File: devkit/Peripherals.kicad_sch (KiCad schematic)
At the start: 50 parts, among them IC501 APDS-9306-065, IC502 BMI270, IC503 LIS2MDLTR, IC504 BMP581, IC505 DRV2603RUNT, IC506 PCA9306JK, IC507 RV-8263-C8, J501 Jumper, J502 Jumper, J503 Jumper, J504 Jumper, J505 Jumper, J506 Jumper, J507 Jumper, M501 Vibrator DC Motor, X501 Current, X502 I2S, X503 Current, X504 I2C, X505 Current, X506 Current, X507 Current, X508 Current, X509 Motor, X510 Current

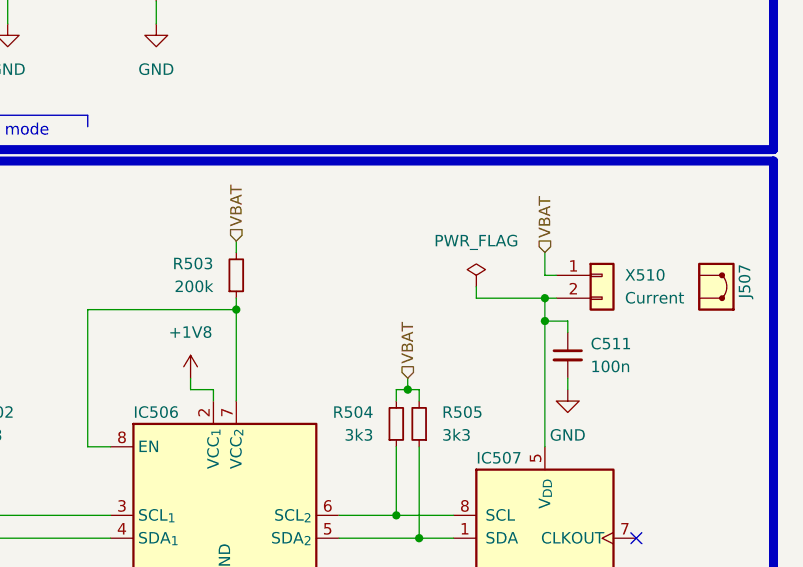
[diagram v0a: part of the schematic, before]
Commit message: Feature: Issue #186
Allow powering RTC from any voltage source

Closes #186

Signed-off-by: Daniel Kampert <DanielKampert@kampis-elektroecke.de>
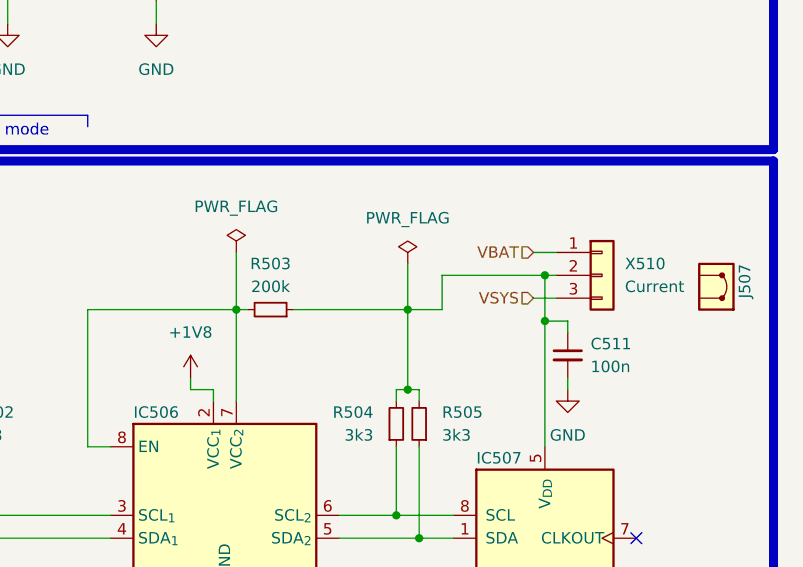
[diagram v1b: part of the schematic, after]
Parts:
- X510: footprint Connector_PinHeader_2.54mm:PinHeader_1x02_P2.54mm_Vertical -> Connector_PinHeader_2.54mm:PinHeader_1x03_P2.54mm_Vertical; symbol Connector_Generic:Conn_01x02 -> Connector_Generic:Conn_01x03; manf# 77311-818-02LF -> 77311-818-03LF; mouser# 649-77311-818-02LF -> 649-77311-818-03LF
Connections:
- net VBAT: no longer R503.2, R504.2, R505.2
- net VSYS: now also X510.3 (Pin_3)
- net at C511.1, IC507.5 (V_{DD}), X510.2 (Pin_2): now also R503.1, R504.2, R505.2
- net at IC506.7 (VCC_{2}), IC506.8 (EN): now also R503.2; no longer R503.1
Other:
- moved on the sheet: R503

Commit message: Revert "Feature: Issue #186"
This reverts commit 73512b60dac517a3d61ff56758c38d705b52f64d.
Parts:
- X510: footprint Connector_PinHeader_2.54mm:PinHeader_1x03_P2.54mm_Vertical -> Connector_PinHeader_2.54mm:PinHeader_1x02_P2.54mm_Vertical; symbol Connector_Generic:Conn_01x03 -> Connector_Generic:Conn_01x02; manf# 77311-818-03LF -> 77311-818-02LF; mouser# 649-77311-818-03LF -> 649-77311-818-02LF
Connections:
- net VBAT: now also R503.2, R504.2, R505.2
- net VSYS: no longer X510.3 (Pin_3)
- net at C511.1, IC507.5 (V_{DD}), X510.2 (Pin_2): no longer R503.1, R504.2, R505.2
- net at IC506.7 (VCC_{2}), IC506.8 (EN): now also R503.1; no longer R503.2
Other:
- moved on the sheet: R503

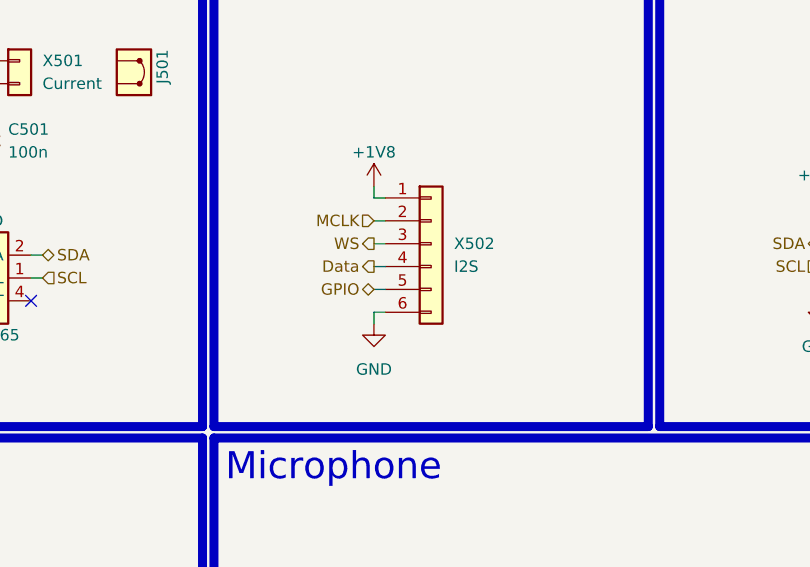
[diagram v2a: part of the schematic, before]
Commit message: Revert "Feature: Issue #180"
This reverts commit 364f4bbc8b17cbfb7f0155205af3315526997ba0.
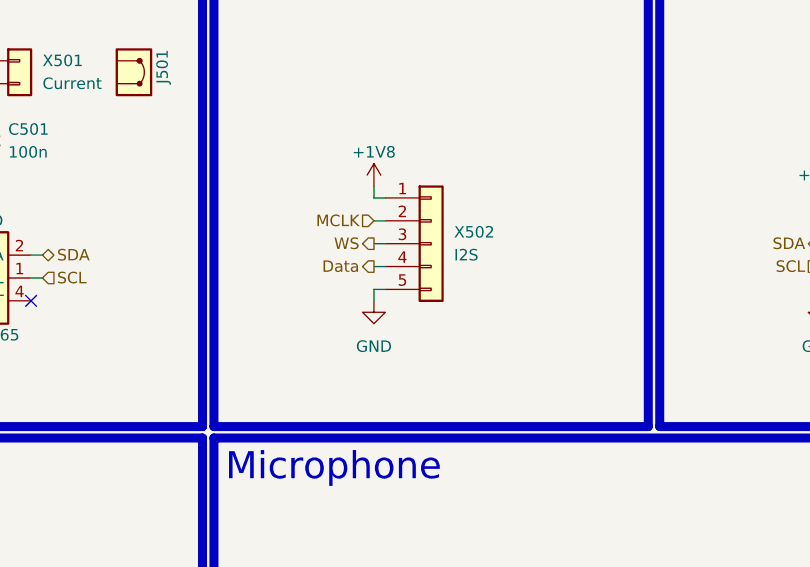
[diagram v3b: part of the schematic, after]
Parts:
- X502: footprint Connector_PinHeader_2.54mm:PinHeader_1x06_P2.54mm_Vertical -> Connector_PinHeader_2.54mm:PinHeader_1x05_P2.54mm_Vertical; symbol Connector_Generic:Conn_01x06 -> Connector_Generic:Conn_01x05; manf# 77311-818-06LF -> 77311-818-05LF; mouser# 649-77311-818-06LF -> 649-77311-818-05LF
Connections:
- net GPIO is gone; now on net GND: X502.5 (Pin_5)
- net GND: no longer X502.6 (Pin_6)
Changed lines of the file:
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@@
 	(wire
 		(pts
-			(xy 80.01 58.42) (xy 78.74 58.42)
+			(xy 80.01 55.88) (xy 78.74 55.88)
 		)
 		(stroke
@@
 	(wire
 		(pts
-			(xy 78.74 58.42) (xy 78.74 59.69)
+			(xy 78.74 55.88) (xy 78.74 57.15)
 		)
 		(stroke
@@
 	(wire
 		(pts
-			(xy 78.74 55.88) (xy 80.01 55.88)
-		)
-		(stroke
-			(width 0)
-			(type default)
-		)
-	)
-	(wire
-		(pts
 			(xy 20.32 111.76) (xy 19.05 111.76)
 		)
@@
 		)
 	)
-	(hierarchical_label "GPIO"
-		(shape bidirectional)
-		(at 78.74 55.88 180)
-		(effects
-			(font
-				(size 1.27 1.27)
-			)
-			(justify right)
-		)
-	)
 	(hierarchical_label "SDA"
 		(shape bidirectional)
@@
 	)
 	(symbol
-		(lib_id "Connector_Generic:Conn_01x06")
+		(lib_id "Connector_Generic:Conn_01x05")
 		(at 85.09 50.8 0)
 		(unit 1)
@@
 		(fields_autoplaced yes)
 		(property "Reference" "X502"
-			(at 87.63 50.7999 0)
+			(at 87.63 49.5299 0)
 			(effects
 				(font
@@
 		)
 		(property "Value" "I2S"
-			(at 87.63 53.3399 0)
+			(at 87.63 52.0699 0)
 			(effects
 				(font
@@
 			)
 		)
-		(property "Footprint" "Connector_PinHeader_2.54mm:PinHeader_1x06_P2.54mm_Vertical"
+		(property "Footprint" "Connector_PinHeader_2.54mm:PinHeader_1x05_P2.54mm_Vertical"
 			(at 85.09 50.8 0)
 			(effects
@@
 			)
 		)
-		(property "Datasheet" "~"
+		(property "Datasheet" "https://cdn.amphenol-cs.com/media/wysiwyg/files/documentation/datasheet/boardwiretoboard/bwb_bergstik.pdf"
 			(at 85.09 50.8 0)
 			(effects
@@
 			)
 		)
-		(property "Description" "Generic connector, single row, 01x06, script generated (kicad-library-utils/schlib/autogen/connector/)"
+		(property "Description" "Generic connector, single row, 01x05, script generated (kicad-library-utils/schlib/autogen/connector/)"
 			(at 85.09 50.8 0)
 			(effects
@@
 			)
 		)
-		(property "manf#" "77311-818-06LF"
+		(property "manf#" "77311-818-05LF"
 			(at 85.09 50.8 0)
 			(effects
@@
 			)
 		)
-		(property "mouser#" "649-77311-818-06LF"
+		(property "mouser#" "649-77311-818-05LF"
 			(at 85.09 50.8 0)
 			(effects
@@
 		(pin "5"
 		)
-		(pin "6"
-		)
 		(instances
 			(project "Dev-Kit"
@@
 	(symbol
 		(lib_id "power:GND")
-		(at 78.74 59.69 0)
+		(at 78.74 57.15 0)
 		(unit 1)
 		(exclude_from_sim no)
@@
 		(dnp no)
 		(property "Reference" "#PWR0506"
-			(at 78.74 66.04 0)
+			(at 78.74 63.5 0)
 			(effects
 				(font
@@
 		)
 		(property "Value" "GND"
-			(at 78.74 64.77 0)
+			(at 78.74 62.23 0)
 			(effects
 				(font
@@
 		)
 		(property "Footprint" ""
-			(at 78.74 59.69 0)
+			(at 78.74 57.15 0)
 			(effects
 				(font
@@
 		)
 		(property "Datasheet" ""
-			(at 78.74 59.69 0)
+			(at 78.74 57.15 0)
 			(effects
 				(font
@@
 		)
 		(property "Description" "Power symbol creates a global label with name \"GND\" , ground"
-			(at 78.74 59.69 0)
+			(at 78.74 57.15 0)
 			(effects
 				(font

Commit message: Feature: Issue #180
- Add additional pin to I2S header

Closes #180

Signed-off-by: Daniel Kampert <DanielKampert@kampis-elektroecke.de>
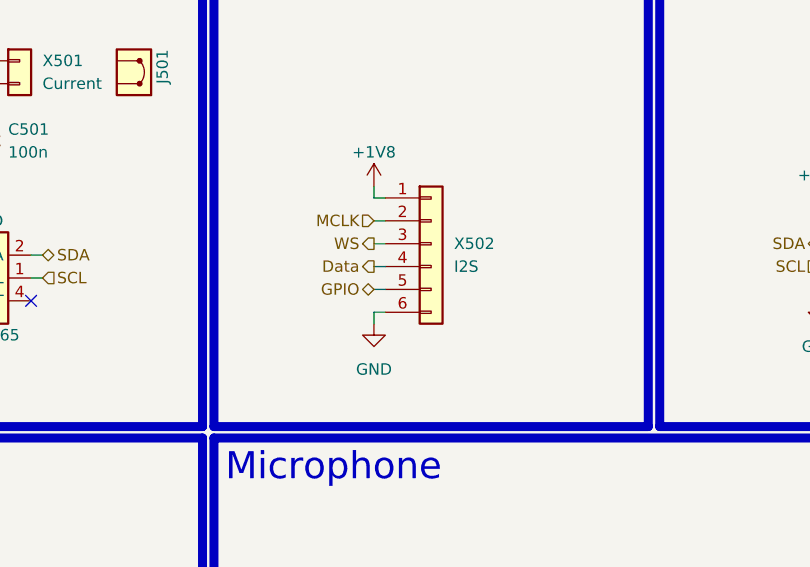
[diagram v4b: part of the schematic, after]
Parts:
- X502: footprint Connector_PinHeader_2.54mm:PinHeader_1x05_P2.54mm_Vertical -> Connector_PinHeader_2.54mm:PinHeader_1x06_P2.54mm_Vertical; symbol Connector_Generic:Conn_01x05 -> Connector_Generic:Conn_01x06; manf# 77311-818-05LF -> 77311-818-06LF; mouser# 649-77311-818-05LF -> 649-77311-818-06LF
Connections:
- net GND: now also X502.6 (Pin_6); no longer X502.5 (Pin_5)
- new net GPIO: X502.5 (Pin_5)
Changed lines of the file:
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@@
 	(wire
 		(pts
-			(xy 80.01 55.88) (xy 78.74 55.88)
+			(xy 80.01 58.42) (xy 78.74 58.42)
 		)
 		(stroke
@@
 	(wire
 		(pts
-			(xy 78.74 55.88) (xy 78.74 57.15)
+			(xy 78.74 58.42) (xy 78.74 59.69)
 		)
 		(stroke
@@
 	(wire
 		(pts
+			(xy 78.74 55.88) (xy 80.01 55.88)
+		)
+		(stroke
+			(width 0)
+			(type default)
+		)
+	)
+	(wire
+		(pts
 			(xy 20.32 111.76) (xy 19.05 111.76)
 		)
@@
 		)
 	)
+	(hierarchical_label "GPIO"
+		(shape bidirectional)
+		(at 78.74 55.88 180)
+		(effects
+			(font
+				(size 1.27 1.27)
+			)
+			(justify right)
+		)
+	)
 	(hierarchical_label "SDA"
 		(shape bidirectional)
@@
 	)
 	(symbol
-		(lib_id "Connector_Generic:Conn_01x05")
+		(lib_id "Connector_Generic:Conn_01x06")
 		(at 85.09 50.8 0)
 		(unit 1)
@@
 		(fields_autoplaced yes)
 		(property "Reference" "X502"
-			(at 87.63 49.5299 0)
+			(at 87.63 50.7999 0)
 			(effects
 				(font
@@
 		)
 		(property "Value" "I2S"
-			(at 87.63 52.0699 0)
+			(at 87.63 53.3399 0)
 			(effects
 				(font
@@
 			)
 		)
-		(property "Footprint" "Connector_PinHeader_2.54mm:PinHeader_1x05_P2.54mm_Vertical"
+		(property "Footprint" "Connector_PinHeader_2.54mm:PinHeader_1x06_P2.54mm_Vertical"
 			(at 85.09 50.8 0)
 			(effects
@@
 			)
 		)
-		(property "Datasheet" "https://cdn.amphenol-cs.com/media/wysiwyg/files/documentation/datasheet/boardwiretoboard/bwb_bergstik.pdf"
+		(property "Datasheet" "~"
 			(at 85.09 50.8 0)
 			(effects
@@
 			)
 		)
-		(property "Description" "Generic connector, single row, 01x05, script generated (kicad-library-utils/schlib/autogen/connector/)"
+		(property "Description" "Generic connector, single row, 01x06, script generated (kicad-library-utils/schlib/autogen/connector/)"
 			(at 85.09 50.8 0)
 			(effects
@@
 			)
 		)
-		(property "manf#" "77311-818-05LF"
+		(property "manf#" "77311-818-06LF"
 			(at 85.09 50.8 0)
 			(effects
@@
 			)
 		)
-		(property "mouser#" "649-77311-818-05LF"
+		(property "mouser#" "649-77311-818-06LF"
 			(at 85.09 50.8 0)
 			(effects
@@
 		(pin "5"
 		)
+		(pin "6"
+		)
 		(instances
 			(project "Dev-Kit"
@@
 	(symbol
 		(lib_id "power:GND")
-		(at 78.74 57.15 0)
+		(at 78.74 59.69 0)
 		(unit 1)
 		(exclude_from_sim no)
@@
 		(dnp no)
 		(property "Reference" "#PWR0506"
-			(at 78.74 63.5 0)
+			(at 78.74 66.04 0)
 			(effects
 				(font
@@
 		)
 		(property "Value" "GND"
-			(at 78.74 62.23 0)
+			(at 78.74 64.77 0)
 			(effects
 				(font
@@
 		)
 		(property "Footprint" ""
-			(at 78.74 57.15 0)
+			(at 78.74 59.69 0)
 			(effects
 				(font
@@
 		)
 		(property "Datasheet" ""
-			(at 78.74 57.15 0)
+			(at 78.74 59.69 0)
 			(effects
 				(font
@@
 		)
 		(property "Description" "Power symbol creates a global label with name \"GND\" , ground"
-			(at 78.74 57.15 0)
+			(at 78.74 59.69 0)
 			(effects
 				(font
